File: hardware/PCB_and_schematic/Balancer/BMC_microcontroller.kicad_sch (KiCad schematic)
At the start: 43 parts, among them J10 Conn_01x03, J11 RS485, J8 ICP, Q1 BC817, Q2 BC817, Q3 BC817, Q4 BC817, U10 PIC16F886-IP, U11 ST485, U12 INA226, U14 TL431LP

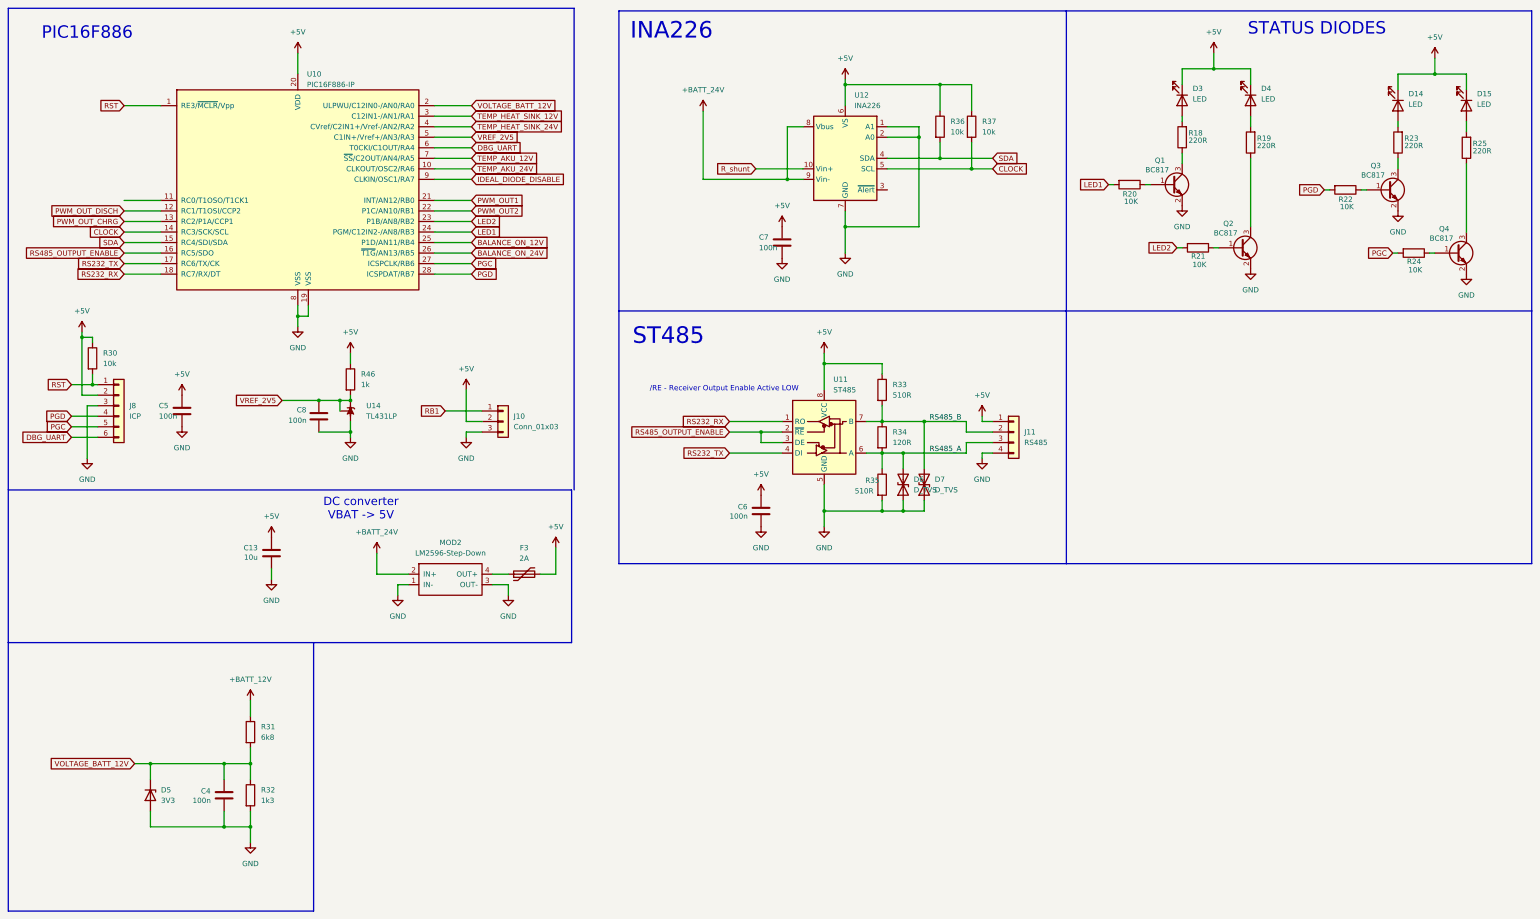
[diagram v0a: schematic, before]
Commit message: add simulations, split bms and esp schematics
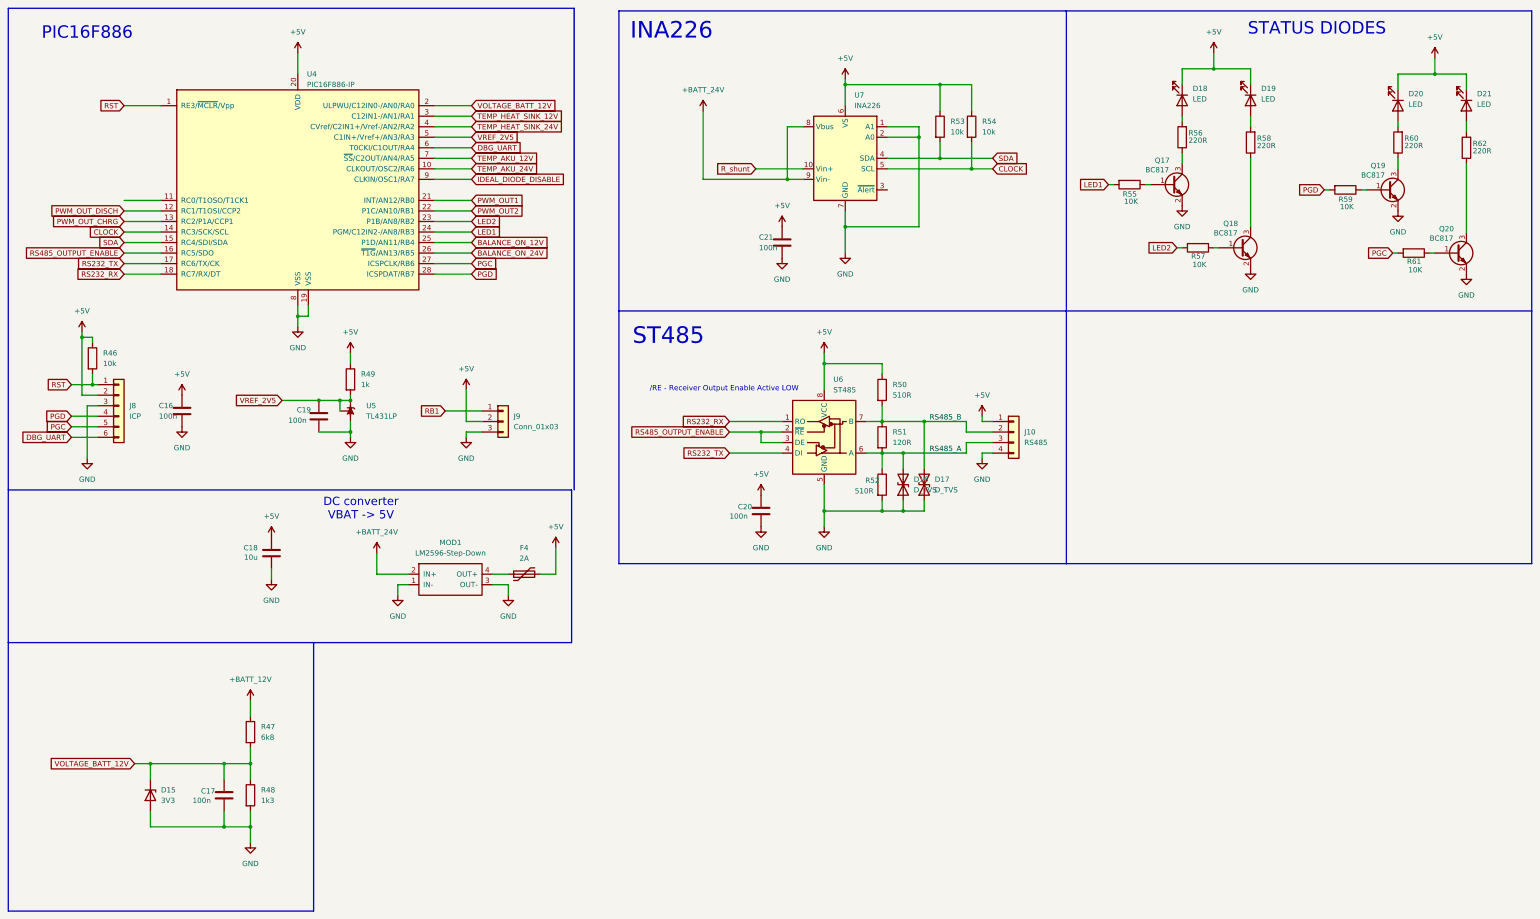
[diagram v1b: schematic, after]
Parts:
- J9: renamed from J10; footprint (none) -> Connector_PinHeader_2.54mm:PinHeader_1x03_P2.54mm_Vertical
- renumbered C5 to C16, C4 to C17, C13 to C18, C8 to C19, C6 to C20, C7 to C21, D5 to D15, D6 to D16, D7 to D17, D3 to D18, D4 to D19, D14 to D20, D15 to D21, F3 to F4, J11 to J10, MOD2 to MOD1, Q1 to Q17, Q2 to Q18, Q3 to Q19, Q4 to Q20, R30 to R46, R31 to R47, R32 to R48, R46 to R49, R33 to R50, R34 to R51, R35 to R52, R36 to R53, R37 to R54, R20 to R55, R18 to R56, R21 to R57, R19 to R58, R22 to R59, R23 to R60, R24 to R61, R25 to R62, U10 to U4, U14 to U5, U11 to U6, U12 to U7
